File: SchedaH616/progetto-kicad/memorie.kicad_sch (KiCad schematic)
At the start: 51 parts, among them J401 DM3AT-SF-PEJM5, U401 MT53E512M32D1ZW-046 IT:B, U402 eMMC 64GB, U403 TPD4E05U06DQA, U404 TPD4E05U06DQA

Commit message: SchedaH616: placement PCB 50x70 a 6 strati e modifiche allo schema
PCB (solo placement, niente piste), generato da generatori/build_pcb.sh:
- 50 x 70 mm, smussi 3 mm, 4 fori NPTH 2.2 mm con keepout, 6 strati
- H616 al centro, LPDDR4 sul lato DRAM, AXP313A vicino alla CPU, eMMC vicino ai pin PC
- connettori sui bordi, U.FL Wi-Fi e SMA GNSS su lati opposti
- disaccoppiamento di H616 e LPDDR4 sul bottom sotto le sfere
- regole: piste 5 mil, via-in-pad 0.25/0.15 sotto l'H616
- DRC: 0 violazioni (solo collegamenti da fare), parità schema/PCB ok

Schema (modifiche approvate):
- LPDDR4 confermata come scelta definitiva
- USB host di nuovo su USB-C solo host (Rp 22k, USBLC6-2, TPS2553)
- jack 5 V diretto su IN1 del TPS2121, tolto l'SS54, TPS56637 in Eco-mode
- LDO AP2112K-1.8 (C176944) dedicato a VCCQ eMMC e VCC_PC
- ERC 0

Libreria H616.pretty: serigrafia sui pad tolta, pioli di centraggio NPTH.

Co-Authored-By: Claude Opus 5.5 (1M context) <noreply@anthropic.com>
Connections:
- net VCC-1V8: no longer C419.1, C420.1, C421.1, R407.1, R408.1, R409.1, R410.1, R411.1, R412.1, R413.1, R414.1, R415.1, R416.1, U402.C6 (VCCQ), U402.M4 (VCCQ), U402.N4 (VCCQ), U402.P3 (VCCQ), U402.P5 (VCCQ)
- new net VCC-1V8-EMMC: C419.1, C420.1, C421.1, R407.1, R408.1, R409.1, R410.1, R411.1, R412.1, R413.1, R414.1, R415.1, R416.1, U402.C6 (VCCQ), U402.M4 (VCCQ), U402.N4 (VCCQ), U402.P3 (VCCQ), U402.P5 (VCCQ)
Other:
- note added: "U402 eMMC 64 GB FBGA-153 (modello da scegliere): VCC = 3V3_PERI, VCCQ = VCC-1V8-EMMC (LDO dedicato, = VCC_PC: HS200, DS per HS400). CLK 33R serie, pull-up 10k su CMD/DAT0-7/RST_n a VCCQ."
- note removed: "U402 eMMC 64 GB FBGA-153 (modello da scegliere): VCC = 3V3_PERI, VCCQ = VCC-1V8 (VCC_PC 1.8 V: HS200, DS per HS400). CLK 33R serie, pull-up 10k su CMD/DAT0-7/RST_n a VCCQ."

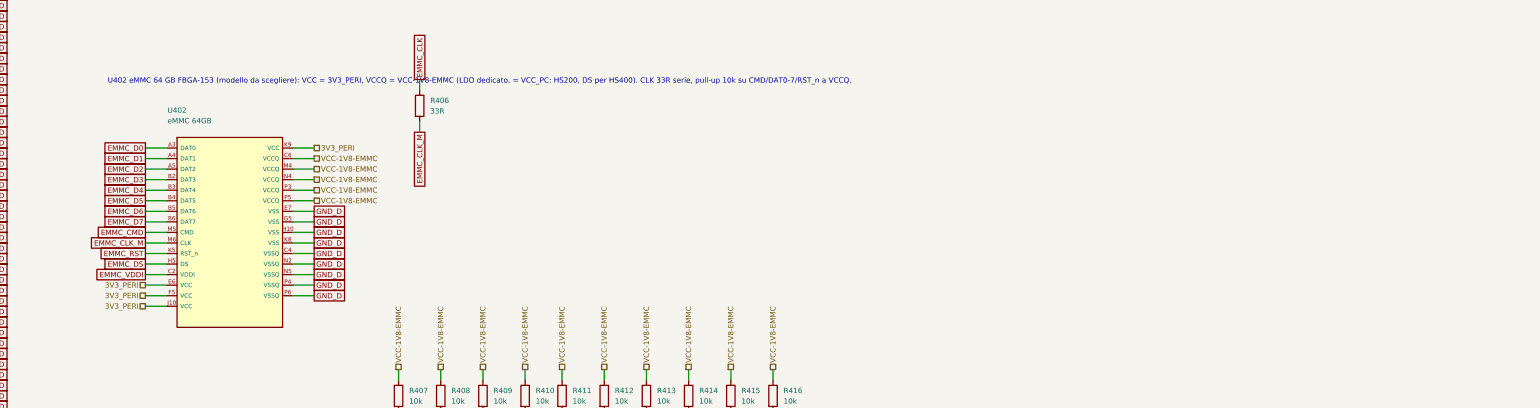
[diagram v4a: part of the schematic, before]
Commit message: SchedaH616: eMMC FORESEE FEMDNN064G-C9A61 (LCSC C49284704)
- U402: valore, MPN e campo LCSC; pinout verificato sul datasheet FORESEE (fig. 2), package JEDEC MO-276 11.5x13 passo 0.5, footprint invariato
- aggiunte a GND le sfere VSS A6 e J5, che mancavano nel simbolo
- campo LCSC portato anche sul PCB; README e scelte-progetto.md aggiornati
- ERC 0, parita' 0, DRC 0 (solo collegamenti da fare)

Co-Authored-By: Claude Opus 5.5 (1M context) <noreply@anthropic.com>
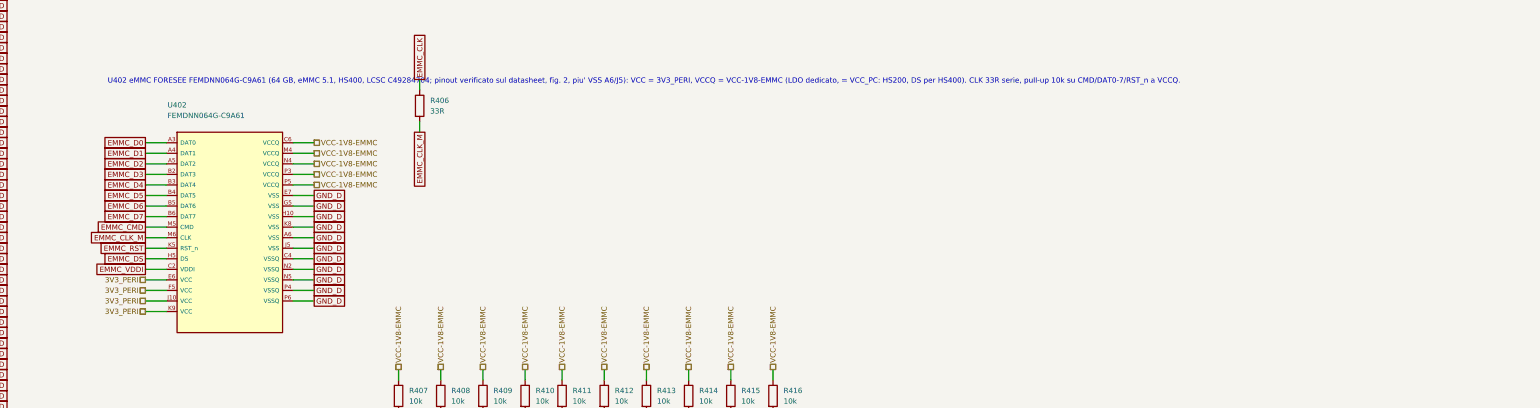
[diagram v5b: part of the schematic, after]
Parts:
- U402: value eMMC 64GB -> FEMDNN064G-C9A61; LCSC (none) -> C49284704; MPN (none) -> FEMDNN064G-C9A61
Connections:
- net GND_D: now also U402.A6 (VSS), U402.J5 (VSS)
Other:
- note added: "U402 eMMC FORESEE FEMDNN064G-C9A61 (64 GB, eMMC 5.1, HS400, LCSC C49284704; pinout verificato sul datasheet, fig. 2, piu' VSS A6/J5): VCC = 3V3_PERI, VCCQ = VCC-1V8-EMMC (LDO dedicato, = VCC_PC: HS200, DS per HS400). CLK 33R serie, pull-up 10k su CMD/DAT0-7/RST_n a VCCQ."
- note removed: "U402 eMMC 64 GB FBGA-153 (modello da scegliere): VCC = 3V3_PERI, VCCQ = VCC-1V8-EMMC (LDO dedicato, = VCC_PC: HS200, DS per HS400). CLK 33R serie, pull-up 10k su CMD/DAT0-7/RST_n a VCCQ."

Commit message: SchedaH616: RK3568 + RK809-5 + TCS4525 + DDR4, placement 50x70
- SoC Allwinner H616 -> Rockchip RK3568 (FCBGA636L, LCSC C2938930): ball map dal pinout
  Rockchip V1.1, verificata sulla tabella 2-1 del datasheet V1.2 (636/636); footprint
  generato (gen_fp.py), confrontato con EasyEDA C2938930
- PMIC AXP313A -> RK809-5 (C2939628) come Rockchip AIoT REF V1.1 / ROCK 3A; TCS4525 per
  VDD_CPU su I2C0 (0x1C); BUCK4 su VDD_NPU (sull'RK809-5 parte spento: non puo' fare il 3.3 V)
- LPDDR4 -> DDR4 x16 K4AAG165WA-BCWE (C2920140) sul canale A, point-to-point, niente VTT,
  VPP da AP2112K-2.5, ZQ 240R, DDR_RZQ del SoC 120R (Hardware Design Guide)
- eMMC su EMMC 8 bit (VCCIO2 1.8 V), microSD su SDMMC0, AP6256 su SDMMC2 + UART8,
  RTL8211F su GMAC0 RGMII (22R TX al SoC e RX al PHY), console UART2_M0, USB-C su OTG0
- Recovery su SARADC_VIN0, reset sulla rete RESETn; TCA6416A tolto
- Bus MIKILAB: BUS_POWER su SPI3_M1, MAIN su SPI2_M1 (CS del DAC su cs-gpios)
- progetto rinominato SchedaRK3568, libreria di progetto Scheda; script portabili Linux/macOS
- ERC 0, parita' 0, DRC 0 (solo collegamenti da fare); placement 439/439

Co-Authored-By: Claude Opus 5.5 (1M context) <noreply@anthropic.com>
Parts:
- removed R423: 10k, Resistor_SMD:R_0402_1005Metric, symbol Device:R
- removed U401: MT53E512M32D1ZW-046 IT:B, Package_BGA:BGA-200_10x14.5mm_Layout12x22_P0.8x0.65mm, symbol H616:LPDDR4_FBGA200
- removed U402: FEMDNN064G-C9A61, Package_BGA:LFBGA-153_11.5x13mm_Layout14x14_P0.5mm, symbol H616:eMMC_FBGA153
- added C424, C425, C427: 0.1uF, Capacitor_SMD:C_0402_1005Metric, symbol Device:C
- added C426: 10uF/10V, Capacitor_SMD:C_0603_1608Metric, symbol Device:C
- added U401: K4AAG165WA-BCWE, Package_BGA:BGA-96_9.0x13.0mm_Layout2x3x16_P0.8mm, symbol Scheda:DDR4_x16_FBGA96
- added U402: FEMDNN064G-C9A61, Package_BGA:LFBGA-153_11.5x13mm_Layout14x14_P0.5mm, symbol Scheda:eMMC_FBGA153
- C401: value 1uF/10V -> 1nF; now not fitted
- C402, C403: value 1uF/10V -> 1nF
- C404: value 1uF/10V -> 10uF; footprint Capacitor_SMD:C_0402_1005Metric -> Capacitor_SMD:C_0603_1608Metric
- C405: value 0.1uF -> 10uF; footprint Capacitor_SMD:C_0402_1005Metric -> Capacitor_SMD:C_0603_1608Metric
- C406, C417: value 0.1uF -> 1uF
- C407, C408, C409, C410, C413, C414, C418: value 0.1uF -> 100nF
- C411, C412, C415: value 1uF/10V -> 100nF
- C416: value 2.2uF/10V -> 100nF
- C419: value 2.2uF/10V -> 1uF/10V
- C420, C423: value 0.1uF -> 2.2uF/10V
- C422: value 10uF/10V -> 0.1uF; footprint Capacitor_SMD:C_0603_1608Metric -> Capacitor_SMD:C_0402_1005Metric
- R401: value 100k 1% -> 240R 1%
- R402: value 100k 1% -> 0R
- R403, R404: value 240R 1% -> 1k 1%; now not fitted
- R405: value 0R -> 22R
- R406: value 33R -> 10k
- R416: value 10k -> 22R
- R417: value 33R -> 47k
- R422: value 47k -> 10k
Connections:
- net EMMC_CLK_M is gone; now on net EMMC_CMD: R406.2
- net LP_ODT_A is gone; now on net GND_D: R401.2
- net LP_ZQ0 is gone; now on net VREF_DDR4_CA: R403.2
- net LP_ZQ1 is gone; now on net GND_D: R404.2
- net VCC-DRAM-FB is gone; now on net EMMC_CLK: R405.2
- net EMMC_CLK: now also U402.M6 (CLK); no longer R406.1
- net EMMC_CMD: now also U402.M5 (CMD); no longer R407.2
- net EMMC_D0: now also R407.2, U402.A3 (DAT0); no longer R408.2
- net EMMC_D1: now also R408.2, U402.A4 (DAT1); no longer R409.2
- net EMMC_D2: now also R409.2, U402.A5 (DAT2); no longer R410.2
- net EMMC_D3: now also R410.2, U402.B2 (DAT3); no longer R411.2
- net EMMC_D4: now also R411.2, U402.B3 (DAT4); no longer R412.2
- net EMMC_D5: now also R412.2, U402.B4 (DAT5); no longer R413.2
- net EMMC_D6: now also R413.2, U402.B5 (DAT6); no longer R414.2
- net EMMC_D7: now also R414.2, U402.B6 (DAT7); no longer R415.2
- net EMMC_DS: now also U402.H5 (DS)
- net EMMC_RST: now also R415.2, U402.K5 (RST_n); no longer R416.2
- net EMMC_VDDI: now also C419.1, U402.C2 (VDDI); no longer C415.1
- net GND_D: now also C424.2, C425.2, C426.2, C427.2, U401.A2 (VSSQ), U401.A8 (VSSQ), U401.B2 (VSS), U401.C9 (VSSQ), U401.D2 (VSSQ), U401.D8 (VSSQ), U401.E1 (VSS), U401.E3 (VSSQ), U401.E8 (VSSQ), U401.E9 (VSS), U401.F1 (VSSQ), U401.G8 (VSS), U401.H1 (VSSQ), U401.H9 (VSSQ), U401.K1 (VSS), U401.K9 (VSS), U401.M9 (VSS), U401.N1 (VSS), U401.N9 (TEN), U401.T1 (VSS), U401.T3 (PAR), U402.A6 (VSS), U402.C4 (VSSQ), U402.E7 (VSS), U402.G5 (VSS), U402.H10 (VSS), U402.J5 (VSS), U402.K8 (VSS), U402.N2 (VSSQ), U402.N5 (VSSQ), U402.P4 (VSSQ), U402.P6 (VSSQ)
- net SD_CLK: now also J401.5 (CLK), R416.2, U403.1 (D1+); no longer R417.1
- net SD_CLK_S: now also R416.1; no longer J401.5 (CLK), R417.2, U403.1 (D1+)
- net SD_CMD: now also R417.2; no longer R418.2
- net SD_D0: now also R418.2; no longer R419.2
- net SD_D1: now also R419.2; no longer R420.2
- net SD_D2: now also R420.2; no longer R421.2
- net SD_D3: now also R421.2; no longer R422.2
- net SD_DET: now also R422.2
- removed net 3V3_PERI: C416.1, C417.1, C418.1, C422.1, C423.1, J401.4 (VDD), R418.1, R419.1, R420.1, R421.1, R422.1
- net LP_ODT_B renamed VREF_DDR4_CA
- net VREF_DDR4_CA: now also C402.1, C403.1, R404.1, U401.M1 (VREFCA)
- net VCC-1V8 renamed VCC_DDR
- net VCC_DDR: now also C404.1, C405.1, C406.1, C407.1, C408.1, C409.1, C410.1, C415.1, C416.1, R403.1, U401.A1 (VDDQ), U401.A9 (VDDQ), U401.B3 (VDD), U401.B9 (VDD), U401.C1 (VDDQ), U401.D1 (VDD), U401.D9 (VDDQ), U401.F2 (VDDQ), U401.F8 (VDDQ), U401.G1 (VDDQ), U401.G7 (VDD), U401.G9 (VDDQ), U401.J1 (VDD), U401.J2 (VDDQ), U401.J8 (VDDQ), U401.J9 (VDD), U401.L1 (VDD), U401.L9 (VDD), U401.R1 (VDD), U401.T9 (VDD)
- net VCC-1V8-EMMC renamed VCC1V8_EMMC
- net VCC1V8_EMMC: now also C423.1, R406.1, C424.1, C425.1, U402.C6 (VCCQ), U402.M4 (VCCQ), U402.N4 (VCCQ), U402.P3 (VCCQ), U402.P5 (VCCQ); no longer C419.1, C420.1, C421.1, R416.1
- removed net VCC-DRAM: C401.1, C402.1, C403.1, C404.1, C405.1, C406.1, C407.1, C408.1, C409.1, C410.1, R401.1, R402.1, R403.1, R404.1, R405.1
- new net DDR4_ZQ: R401.1, U401.F9 (ZQ)
- new net DDR_A0: U401.P3 (A0)
- new net DDR_A1: U401.P7 (A1)
- new net DDR_A10: U401.M3 (A10/AP)
- new net DDR_A11: U401.T2 (A11)
- new net DDR_A12: U401.M7 (A12/BC_n)
- new net DDR_A13: U401.T8 (A13)
- new net DDR_A14_WE_N: U401.L2 (WE_n/A14)
- new net DDR_A15_CAS_N: U401.M8 (CAS_n/A15)
- new net DDR_A16_RAS_N: U401.L8 (RAS_n/A16)
- new net DDR_A2: U401.R3 (A2)
- new net DDR_A3: U401.N7 (A3)
- new net DDR_A4: U401.N3 (A4)
- new net DDR_A5: U401.P8 (A5)
- new net DDR_A6: U401.P2 (A6)
- new net DDR_A7: U401.R8 (A7)
- new net DDR_A8: U401.R2 (A8)
- new net DDR_A9: U401.R7 (A9)
- new net DDR_ACT_N: U401.L3 (ACT_n)
- new net DDR_BA0: U401.N2 (BA0)
- new net DDR_BA1: U401.N8 (BA1)
- new net DDR_BG0: U401.M2 (BG0)
- new net DDR_CKE: U401.K2 (CKE)
- new net DDR_CK_N: U401.K8 (CK_c)
- new net DDR_CK_P: U401.K7 (CK_t)
- new net DDR_CS_N: U401.L7 (CS_n)
- new net DDR_DML: U401.E7 (DML_n/DBIL_n)
- new net DDR_DMU: U401.E2 (DMU_n/DBIU_n)
- new net DDR_DQL0: U401.G2 (DQL0)
- new net DDR_DQL1: U401.F7 (DQL1)
- new net DDR_DQL2: U401.H3 (DQL2)
- new net DDR_DQL3: U401.H7 (DQL3)
- new net DDR_DQL4: U401.H2 (DQL4)
- new net DDR_DQL5: U401.H8 (DQL5)
- new net DDR_DQL6: U401.J3 (DQL6)
- new net DDR_DQL7: U401.J7 (DQL7)
- new net DDR_DQSL_N: U401.F3 (DQSL_c)
- new net DDR_DQSL_P: U401.G3 (DQSL_t)
- new net DDR_DQSU_N: U401.A7 (DQSU_c)
- new net DDR_DQSU_P: U401.B7 (DQSU_t)
- new net DDR_DQU0: U401.A3 (DQU0)
- new net DDR_DQU1: U401.B8 (DQU1)
- new net DDR_DQU2: U401.C3 (DQU2)
- new net DDR_DQU3: U401.C7 (DQU3)
- new net DDR_DQU4: U401.C2 (DQU4)
- new net DDR_DQU5: U401.C8 (DQU5)
- new net DDR_DQU6: U401.D3 (DQU6)
- new net DDR_DQU7: U401.D7 (DQU7)
- new net DDR_ODT: U401.K3 (ODT)
- new net DDR_RESET_N: C401.1, U401.P1 (RESET_n)
- new net DDR_VREFOUT: R402.1
- new net EMMC_CLK_S: R405.1
- new net VCC2V5_DDR: C417.1, C418.1, U401.B1 (VPP), U401.R9 (VPP)
- new net VCC3V3_PMU: R422.1
- new net VCC3V3_SD: C426.1, C427.1, J401.4 (VDD)
- new net VCCIO_SD: R417.1, R418.1, R419.1, R420.1, R421.1
- new net VCC_3V3: C420.1, C421.1, C422.1, U402.E6 (VCC), U402.F5 (VCC), U402.J10 (VCC), U402.K9 (VCC)
- no-connect marks 26 -> 11
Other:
- note added: "DQ/DM/DQS secondo il pinout Rockchip (DDR_DQx_A -> DDR4_DQL/DQU_A): l'ordine dei bit nel byte e' quello del template Rockchip, i CA non si possono scambiare (Hardware Design Guide 2.1.7)."
- note added: "Disaccoppiamento DDR4 (reference, ridotto a un chip): VCC_DDR 2x 10 uF + 1 uF + 10x 100 nF; VPP 1 uF + 100 nF vicino alle sfere B1/R9."
- note added: "J401 microSD (Hirose DM3AT) su SDMMC0: VDD = VCC3V3_SD (SWOUT2 dell'RK809-5), segnali a VCCIO_SD (LDO5, 3.3 V, 1.8 V per UHS). CLK 22R serie, pull-up 47k a VCCIO_SD."
- note added: "MEMORIE: DDR4 x16 (1 chip, point-to-point, niente VTT), eMMC 8 bit su EMMC (VCCIO2 1.8 V), microSD su SDMMC0 (VCCIO3). Serie 4xx."
- note added: "SD_DET su SDMMC0_DET (GPIO0_A4, PMUIO1) con 10k a VCC3V3_PMU: basso con la scheda inserita = SDMMC0 (alto = JTAG sui pin SDMMC0, Hardware Design Guide)."
- note added: "U401 Samsung K4AAG165WA-BCWE (LCSC C2920140, 16 Gbit = 2 GB, x16, DDR4-3200): VDD/VDDQ = VCC_DDR 1.2 V (BUCK3), VPP = VCC2V5_DDR (AP2112K-2.5). Collegata al canale A del PHY dell'RK3568."
- note added: "U402 eMMC FORESEE FEMDNN064G-C9A61 (64 GB, eMMC 5.1 HS400, LCSC C49284704): VCC = VCC_3V3, VCCQ = VCC1V8_EMMC (AP2112K-1.8, = VCCIO2: HS200/HS400). CLK 22R serie vicino al SoC (reference), pull-up 10k su CMD/DAT0-7/RST_n."
- note added: "VREFCA da DDR_VREFOUT del SoC (P8, 0.6 V di default) con 0R; 2x 1 nF vicino alla DDR4 (valore da non cambiare, Hardware Design Guide). Partitore 1k/1k DNP come alternativa."
- note added: "ZQ 240R 1% a GND, TEN e PAR a GND, ALERT_n libero, T7 (NC/A17) libero (reference Rockchip DDR4 16bit SDP). RESET_n con 1 nF DNP (anti-ESD, Hardware Design Guide)."
- note removed: "CA0 <- SA1, CA1 <- SCS0, CA2 <- SA0, CA3 <- SCS1, CA4 <- SA4, CA5 <- SA3, CS0 <- SA2, CS1 <- SA5 (da phy_init U-Boot, NON VERIFICATO). DQ dritti: canale A = byte 0-1, canale B = byte 2-3."
- note removed: "Disaccoppiamento LPDDR4: VDD2/VDDQ 4x1uF + 6x0.1uF, VDD1 2x1uF + 2x0.1uF (da rifinire con la PDN Micron)."
- note removed: "J401 microSD (Hirose DM3AT) su SMHC0: VDD = 3V3_PERI (solo 3.3 V, niente UHS), CLK 33R serie, pull-up 47k a 3V3_PERI. SD_DET sull'espansore (P15), 10k a VCC-IO."
- note removed: "MEMORIE: LPDDR4 2 GB x32 (1 chip, come Orange Pi Zero3), eMMC 8 bit su SMHC2 (PC, 1.8 V), microSD su SMHC0 (PF, 3.3 V). Serie 4xx."
- note removed: "ODT_CA_A/B a VDD2 con 100k, ZQ0/ZQ1 240R 1% a VDDQ (come il reference Allwinner). CS1/CKE1 su sfere NC del chip a singolo rank."
- note removed: "R405: sense del DCDC3 dell'AXP313A preso sulle sfere VDD2 della LPDDR4."
- note removed: "U401 MT53E512M32D1ZW-046 IT:B: 1 die, 2 canali x16, CA comuni ai due canali. VDD1 = VCC-1V8 (ALDO1), VDD2/VDDQ = VCC-DRAM 1.1 V (DCDC3). Niente VTT/VREF/VPP."
- note removed: "U402 eMMC FORESEE FEMDNN064G-C9A61 (64 GB, eMMC 5.1, HS400, LCSC C49284704; pinout verificato sul datasheet, fig. 2, piu' VSS A6/J5): VCC = 3V3_PERI, VCCQ = VCC-1V8-EMMC (LDO dedicato, = VCC_PC: HS200, DS per HS400). CLK 33R serie, pull-up 10k su CMD/DAT0-7/RST_n a VCCQ."
